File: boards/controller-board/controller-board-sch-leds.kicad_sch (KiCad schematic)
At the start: 151 parts, among them IC10 A6214KLKTR-T, IC11 A6214KLKTR-T, IC12 A6214KLKTR-T, IC13 A6214KLKTR-T, IC2 A6214KLKTR-T, IC3 A6214KLKTR-T, IC4 A6214KLKTR-T, IC5 A6214KLKTR-T, IC6 A6214KLKTR-T, IC7 A6214KLKTR-T, IC8 A6214KLKTR-T, IC9 A6214KLKTR-T

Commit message: completed layout for new LED drivers in schematic
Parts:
- removed C34, C35, C37, C38, C39, C40: 100n, oresat-passives:0603-C-NOSILK, symbol Device:C_Small
- removed C36: 100n, oresat-passives:0402-C-NOSILK, symbol Device:C_Small
- removed C41, C42, C43, C50, C51, C57, C58, C59, C60, C61, C62, C64: 10u, oresat-passives:1206-C, symbol Device:C_Small
- removed C44, C45, C46, C47, C48, C49, C52, C53, C54, C55, C56, C63: 1u, oresat-passives:0603-C-NOSILK, symbol Device:C_Small
- removed D1, D10, D11, D2, D3, D4, D41, D5, D6, D7, D8, D9: VS-10MQ060NTRPBF, Diode_SMD:D_SMA, symbol Device:D_Schottky
- removed D47, D48, D57, D58, D59, D64: XPEBRD-L1-0000-00501, oresat-diodes:Cree-LED, symbol Device:LED_Pad
- removed D49, D50, D51, D52, D60, D61: XPEBGR-L1-0000-00D01, oresat-diodes:Cree-LED, symbol Device:LED_Pad
- removed D53, D54, D55, D56, D62, D63, D71, D72, D73, D74, D83, D84: XPEBBL-L1-0000-00201, oresat-diodes:Cree-LED, symbol Device:LED_Pad
- removed D75, D76, D79, D80: UVA LED, oresat-diodes:LED-Everlight-1414-UVA, symbol Device:LED_Pad
- removed D86: UVC LED, oresat-diodes:Cree-LED, symbol Device:LED_Pad
- removed D88: UVC LED, oresat-diodes:LED-Everlight-1414-UVC, symbol Device:LED_Pad
- removed IC10, IC11, IC12, IC13, IC2, IC3, IC4, IC5, IC6, IC7, IC8, IC9: A6214KLKTR-T, oresat-ics:SOP100P600X165-11N, symbol oresat-ics:A6214KLKTR-T
- removed L10, L11, L12, L18, L8, L9: 47u, Inductor_SMD:L_Coilcraft_MSS1048-XXX, symbol Device:L_Small
- removed R24, R25, R26, R27, R28, R29, R30, R31, R32, R34, R35: 95.3k, oresat-passives:0603-C-NOSILK, symbol Device:R_Small_US
- removed R33: 2, oresat-passives:0603-C-NOSILK, symbol Device:R_Small_US
- removed R36, R37, R38, R39, R40, R41, R42, R43, R44, R45, R46, R47: 1k, oresat-passives:0603-C-NOSILK, symbol Device:R_Small_US
- added D1, D10, D11, D12, D13, D14, D15, D16, D17, D18, D2, D3, D4, D5, D6, D7, D8, D9: LED, oresat-diodes:Cree-XLAMP-XE-G-LEDs, symbol oresat-diodes:LED_WITH_GND_PAD
- added U10, U11, U6, U7, U8, U9: MP2410A, Package_TO_SOT_SMD:TSOT-23-6, symbol oresat-ics:MP2410A_LED_Driver
- C11, C13, C14, C20, C21, C24, C27: value 100n -> 10u; footprint oresat-passives:0402-C-NOSILK -> oresat-passives:1206-C; DPN 490-6328-1-ND -> 1276-6767-1-ND; Distributor DigiKey -> (none); MFR Murata Electronics -> (none); MPN GRM155R71C104KA88J -> (none)
- C12, C23, C25, C29: value 100n -> 10n; footprint oresat-passives:0402-C-NOSILK -> oresat-passives:0603-C-NOSILK; DPN 490-6328-1-ND -> 478-KGM15AR71H103KTCT-ND; Distributor DigiKey -> (none); MFR Murata Electronics -> (none); MPN GRM155R71C104KA88J -> (none)
- C22, C28, C30, C31, C33: value 100n -> 10u; footprint oresat-passives:0603-C-NOSILK -> oresat-passives:1206-C; DPN 490-6328-1-ND -> 1276-6767-1-ND; Distributor DigiKey -> (none); MFR Murata Electronics -> (none); MPN GRM155R71C104KA88J -> (none)
- C26: value 100n -> 10n; DPN 490-6328-1-ND -> 478-KGM15AR71H103KTCT-ND; Distributor DigiKey -> (none); MFR Murata Electronics -> (none); MPN GRM155R71C104KA88J -> (none)
- C32: value 470u -> 10n; footprint Capacitor_SMD:CP_Elec_10x12.5 -> oresat-passives:0603-C-NOSILK; DPN 56-MAL215097012E3CT-ND -> 478-KGM15AR71H103KTCT-ND; Distributor DigiKey -> (none); MFR Vishay Beyschlag/Draloric/BC Components -> (none); MPN MAL215097012E3 -> (none)
- L2, L3, L4, L6: value 47u -> 3.2u; footprint Inductor_SMD:L_Coilcraft_MSS1048-XXX -> oresat-passives:Inductor Coilcraft DO1813H-332 3.2uH; DPN 308-1641-1-ND -> 2457-DO1813H-332MLD-ND; Distributor DigiKey -> (none); MFR Sumida America Components Inc. -> (none); MPN CDRH105RNP-470NC -> (none)
- L5, L7: value 47u -> 2.6u; footprint Inductor_SMD:L_Coilcraft_MSS1048-XXX -> oresat-passives:Ind 2.6u 2A; DPN 308-1641-1-ND -> SRR5028-2R6YCT-ND; Distributor DigiKey -> (none); MFR Sumida America Components Inc. -> (none); MPN CDRH105RNP-470NC -> (none)
- R11, R14, R15, R19: value .576 -> 50m; footprint oresat-passives:0603-C-NOSILK -> oresat-passives:1206-C; DPN 2019-SR731JRTTDR576FCT-ND -> 273-KDV12DR050ETCT-ND; Distributor DigiKey -> (none); MFR KOA Speer Electronics, Inc. -> (none); MPN SR731JRTTDR576F -> (none)
- R16, R17, R18, R6: value .576 -> 1k; DPN 2019-SR731JRTTDR576FCT-ND -> 311-1.00KHRCT-ND; Distributor DigiKey -> (none); MFR KOA Speer Electronics, Inc. -> (none); MPN SR731JRTTDR576F -> (none)
- R20: value 0.430 -> 1k; DPN P17399CT-ND -> 311-1.00KHRCT-ND; Distributor ERJ-3BQFR43V -> (none); MFR Panasonic Electronic Components -> (none); MPN ERJ-3BQFR43V -> (none)
- R21: value 2 -> 50m; footprint oresat-passives:0603-C-NOSILK -> oresat-passives:1206-C; DPN 311-2.00HRCT-ND -> 273-KDV12DR050ETCT-ND; Distributor DigiKey -> (none); MFR YAGEO -> (none); MPN RC0603FR-072RL -> (none)
- R22: value 0.430 -> 1k; DPN P17399CT-ND -> 311-1.00KHRCT-ND; Distributor DigiKey -> (none); MFR Panasonic Electronic Components -> (none); MPN ERJ-3BQFR43V -> (none)
- R23: value 95.3k -> 50m; footprint oresat-passives:0603-C-NOSILK -> oresat-passives:1206-C; DPN YAG4607CT-ND -> 273-KDV12DR050ETCT-ND; Distributor DigiKey -> (none); MFR Yageo -> (none); MPN RT0603BRD0795K3L -> (none)
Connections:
- net +12V: now also C11.1, C14.1, C20.1, C24.1, C28.1, C31.1, U10.3 (VIN), U11.3 (VIN), U6.3 (VIN), U7.3 (VIN), U8.3 (VIN), U9.3 (VIN); no longer C32.1, R23.1
- net GND: now also C11.2, C14.2, C20.2, C24.2, R11.2, R14.2, R15.2, R19.2, R21.2, R23.2, D1.3 (pad), D10.3 (pad), D11.3 (pad), D12.3 (pad), D13.3 (pad), D14.3 (pad), D15.3 (pad), D16.3 (pad), D17.3 (pad), D18.3 (pad), D2.3 (pad), D3.3 (pad), D4.3 (pad), D5.3 (pad), D6.3 (pad), D7.3 (pad), D8.3 (pad), D9.3 (pad), U10.1 (GND), U11.1 (GND), U6.1 (GND), U7.1 (GND), U8.1 (GND), U9.1 (GND); no longer C22.2, C26.2, C30.2, C32.2, C33.2
- net at C21.1: now also L5.2, D7.2 (A); no longer L3.1
- net at L3.2: now also C27.1, D10.2 (A); no longer R17.1
- net at R20.2: now also C30.2, R21.1, D15.1 (K)
- net at L6.1: now also C29.2, U10.2 (SW); no longer C11.1
- net at R11.1: now also C13.2, R6.2, D3.1 (K); no longer L6.2
- net at R18.2: now also C27.2, R19.1, D12.1 (K)
- net at C29.1: now also U10.6 (BST)
- net at R22.1: now also U11.4 (FB)
- net at R14.1: now also C22.2, R16.2, D6.1 (K); no longer L7.2
- net at L2.1: now also C12.2, U6.2 (SW); no longer C20.1
- net at R18.1: now also U7.4 (FB); no longer L2.2
- net at L5.1: now also C26.2, U9.2 (SW)
- net at R6.1: now also U6.4 (FB); no longer L5.2
- net at R17.2: now also C21.2, R15.1, D9.1 (K)
- net at C26.1: now also U9.6 (BST); no longer R21.2
- net at C33.1: now also L7.2, D16.2 (A); no longer R15.2
- net at C23.1: now also U8.6 (BST); no longer L4.1
- net at C22.1: now also L4.2, D4.2 (A); no longer R16.2
- net at R16.1: now also U8.4 (FB); no longer L4.2
- net at C23.2: now also L4.1, U8.2 (SW)
- net at C13.1: now also L2.2, D1.2 (A)
- net at R22.2: now also C33.2, R23.1, D18.1 (K); no longer C30.1
- net at C25.1: now also U7.6 (BST)
- net at C25.2: now also L3.1, U7.2 (SW)
- net at L7.1: now also C32.2, U11.2 (SW); no longer C12.1
- net at R20.1: now also U10.4 (FB)
- new net: D17.1 (K), D18.2 (A)
- new net: D16.1 (K), D17.2 (A)
- new net: D2.1 (K), D3.2 (A)
- new net: D11.1 (K), D12.2 (A)
- new net: D10.1 (K), D11.2 (A)
- new net: D14.1 (K), D15.2 (A)
- new net: R17.1, U9.4 (FB)
- new net: D5.1 (K), D6.2 (A)
- new net: D4.1 (K), D5.2 (A)
- new net: D13.1 (K), D14.2 (A)
- new net: C32.1, U11.6 (BST)
- new net: C30.1, D13.2 (A), L6.2
- new net: D8.1 (K), D9.2 (A)
- new net: D7.1 (K), D8.2 (A)
- new net: D1.1 (K), D2.2 (A)
- new net: C12.1, U6.6 (BST)
- new net Cyan_LED: U10.5 (EN/DIM), U8.5 (EN/DIM)
- new net Violet_LED: U11.5 (EN/DIM), U9.5 (EN/DIM)
- new net White_LED: U6.5 (EN/DIM), U7.5 (EN/DIM)
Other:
- note added: "FB capacitor value from eval board Bootstrap capacitor value from eval board"
- note added: "all capacitors 50V+"
- note removed: "Blue LED Channel"
- note removed: "Bypass Capacitor (parallel caps from LED drivers in one)"
- note removed: "Green LED Channel"
- note removed: "Red LED Channel"
- note removed: "UV LED Channel"
- note removed: "check that chosen 470u cap is good for design"

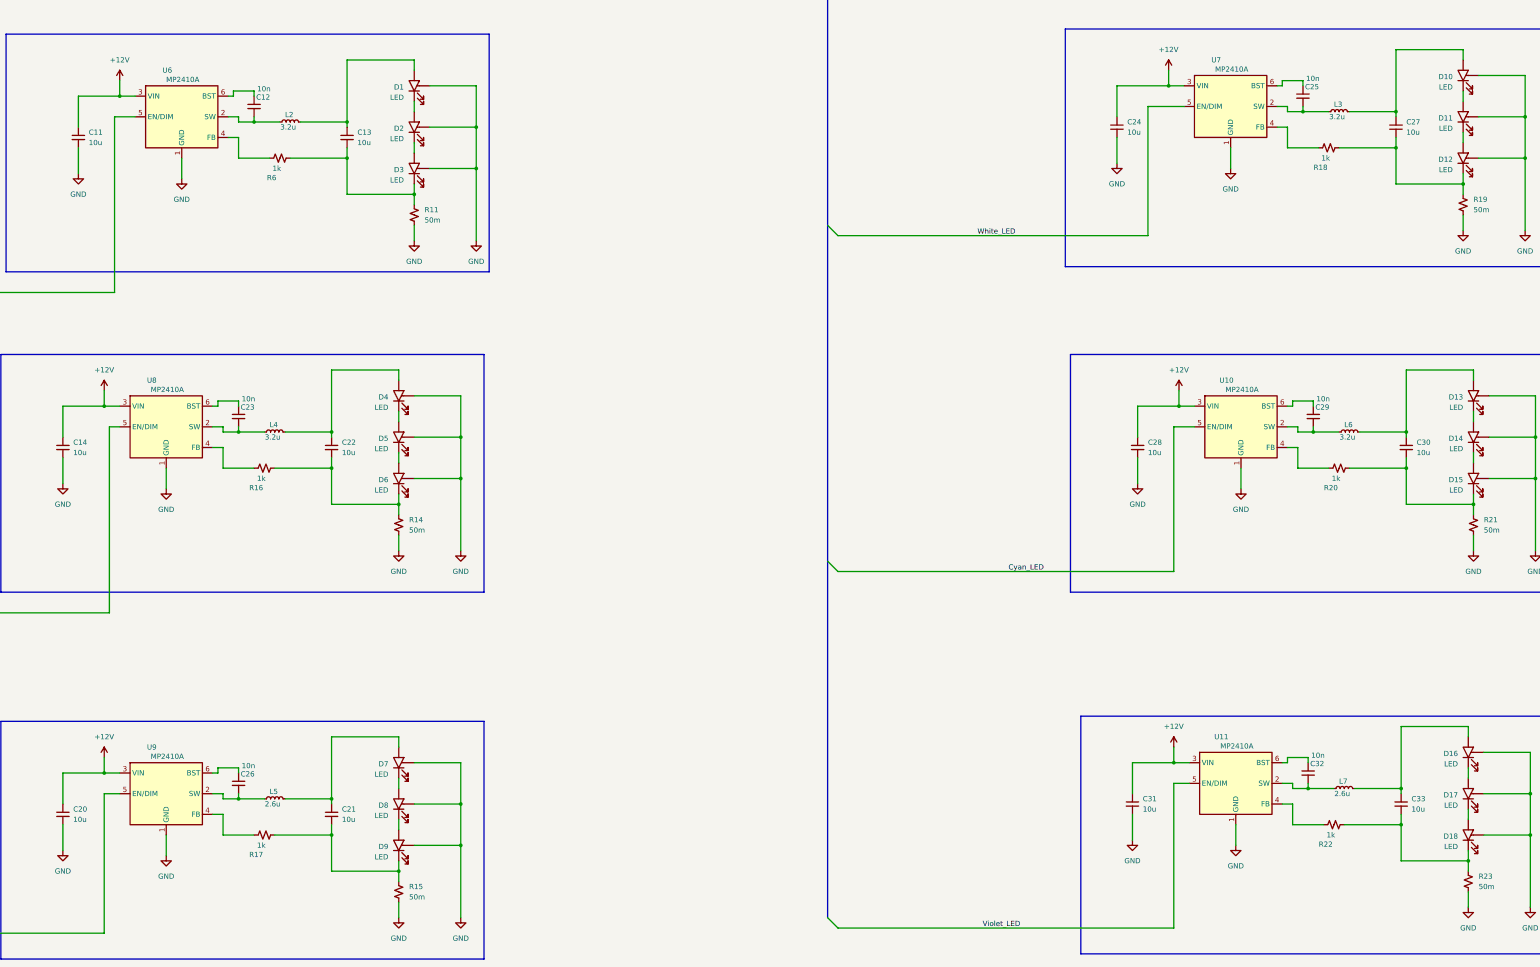
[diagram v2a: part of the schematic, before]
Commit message: modified pcb layout: rotated halogen circuitry block and moved power input for halogen closer to light halogen light, moved thermistor block, moved power input pin onto zone connecting to halogen block, replaced track connecting pin 2 on LED drivers to indcutors with thicker track and zones
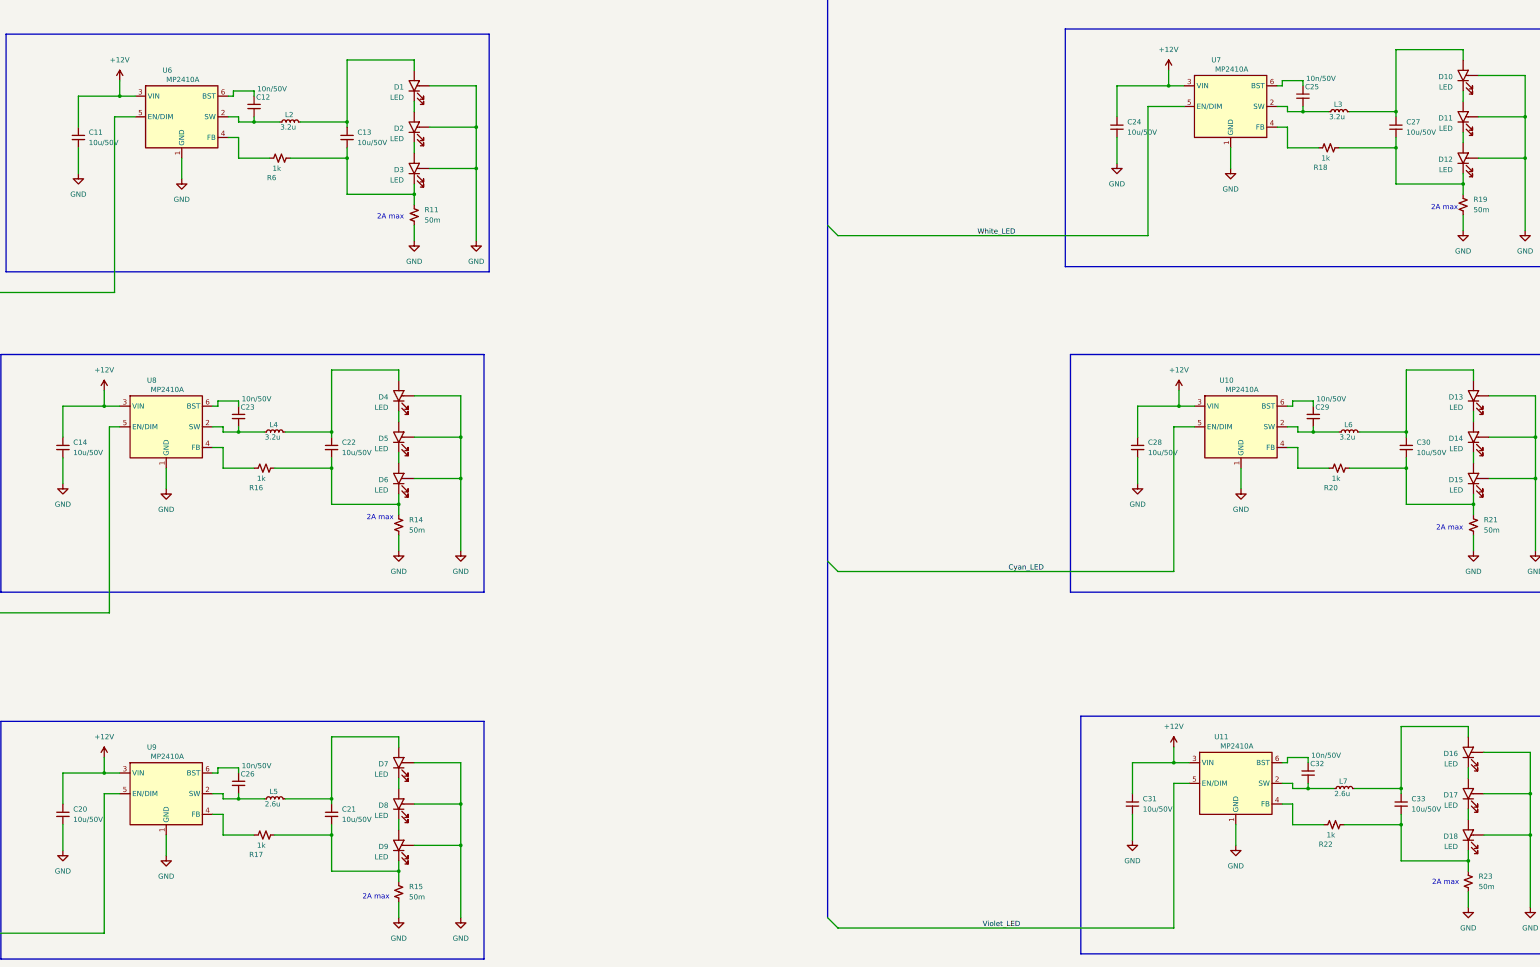
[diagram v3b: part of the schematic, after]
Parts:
- C11, C13, C14, C20, C21, C22, C24, C27, C28, C30, C31, C33: value 10u -> 10u/50V; Distributor (none) -> DigiKey; MFR (none) -> Samsung Electro-Mechanics; MPN (none) -> CL31B106KBHNNNE
- C12, C23, C25, C26, C29, C32: value 10n -> 10n/50V; Distributor (none) -> DigiKey; MFR (none) -> KYOCERA AVX; MPN (none) -> KGM15AR71H103KT
- D1, D10, D11, D12, D2, D3: Distributor (none) -> DigiKey; MFR (none) -> Cree LED; MPN (none) -> XEGAWT-H0-0000-000-000000U30DT
- D13, D14, D15, D4, D5, D6: Distributor (none) -> DigiKey; MFR (none) -> Cree LED; MPN (none) -> XEGAPC-H0-0000-000-000000U2001
- D16, D17, D18, D7, D8, D9: Distributor (none) -> DigiKey; MFR (none) -> Cree LED; MPN (none) -> XEGAVT-H2-0000-000-000000K2001
- L2, L3, L4, L6: Distributor (none) -> DigiKey; MFR (none) -> Coilcraft; MPN (none) -> DO1813H-332MLD
- L5, L7: Distributor (none) -> DigiKey; MFR (none) -> Bourns Inc.; MPN (none) -> SRR5028-2R6Y
- R16, R17, R18, R20, R22, R6: Distributor (none) -> DigiKey; MFR (none) -> Yageo; MPN (none) -> RC0603FR-071KL
- U10, U11, U6, U7, U8, U9: DPN (none) -> 1589-1584-1-ND; Distributor (none) -> DigiKey; MFR (none) -> Monolithic Power Systems Inc.; MPN (none) -> MP2410AGJ-Z
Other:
- note added: "2A max"

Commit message: Updated 3D models, ground stitching, zone layout, lots of polishing and checking before fab.
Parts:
- D1, D10, D11, D12, D2, D3: value LED -> WHITE
- D13, D14, D15, D4, D5, D6: value LED -> PC CYAN
- D16, D17, D18, D7, D8, D9: value LED -> VIOLET
- R11, R14, R15, R19, R21, R23: Distributor (none) -> DigiKey; MFR (none) -> Ohmite; MPN (none) -> KDV12DR050ET
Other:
- moved on the sheet: C11, C12, C13, C14, C20, C21, C22, C23, C24, C25, C26, C27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
